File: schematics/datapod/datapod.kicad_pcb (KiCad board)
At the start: 2 copper layers, 152.7 x 152.7 mm, 56 parts, among them J1 Conn_01x02, J2 Conn_02x03_Odd_Even, J3 Conn_01x02, J4 DB9_Female, J5 DB9_Male_MountingHoles, J6 Micro_SD_Card, J7 Conn_02x02_Odd_Even, J8 Conn_01x02_Female, K1 DS2E-SL2-DC5V, K2 DS2E-SL2-DC5V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

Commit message: made 1st pcb
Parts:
- moved J3 106.8 mm to (123.2, 149.9), turned to 203 degrees
- moved D3 105.4 mm to (114.3, 25.4), turned to 0 degrees
- moved J7 102.8 mm to (48.3, 141.0), turned to 45 degrees
- moved C1 97.3 mm to (144.6, 119.3), turned to 315 degrees
- moved J8 92.8 mm to (48.3, 59.7), turned to 236 degrees
- moved D1 92.3 mm to (85.6, 149.9), turned to 180 degrees
- moved Q4 90.7 mm to (158.8, 135.9)
- moved D4 87.8 mm to (110.5, 52.6), turned to 270 degrees
- moved D5 87.2 mm to (72.1, 75.3)
- moved C17 85.0 mm to (82.4, 62.1), turned to 90 degrees
- moved C14 84.9 mm to (73.2, 78.9)
- moved Q2 84.0 mm to (120.7, 61.0)
- moved RN1 82.9 mm to (158.8, 124.5), turned to 180 degrees
- moved C7 81.9 mm to (167.6, 122.9), turned to 90 degrees
- moved Q3 80.4 mm to (151.1, 108.0), turned to 180 degrees
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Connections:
- RN1 pad 10: VcR1 -> Net-(RN1-Pad10)
- RN3 pad 10: Net-(RN3-Pad10) -> VcR1
- RN3 pad 11: Net-(RN3-Pad11) -> GND
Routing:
- net VCC: track 0.00 -> 122.9 mm, vias 0 -> 3
- net GND: track 0.00 -> 99.7 mm
- net Net-(C12-Pad2): track 0.00 -> 49.5 mm
- net RELAY2_OFF: track 0.00 -> 43.4 mm, vias 0 -> 2
- net +5V: track 0.00 -> 40.9 mm, vias 0 -> 4
- net +3V3: track 0.00 -> 40.5 mm, vias 0 -> 1
- net RELAY2_ON: track 0.00 -> 25.3 mm, vias 0 -> 1
- net MICRO_SD_MOSI: track 0.00 -> 24.1 mm
- net Net-(J4-Pad2): track 0.00 -> 17.9 mm
- net Net-(J4-Pad3): track 0.00 -> 17.3 mm
- net Net-(C2-Pad1): track 0.00 -> 16.9 mm
- net MCU-SDA: track 0.00 -> 16.6 mm
- net MICRO_SD_MISO: track 0.00 -> 15.9 mm
- net Net-(C10-Pad2): track 0.00 -> 15.4 mm
- net MICRO_SD_SCK: track 0.00 -> 15.3 mm
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- added copper zone on F.Cu, net +3V3
- added copper zone on F.Cu, net +5V
- added copper zone on F.Cu, net Net-(C14-Pad2)
- added copper zone on F.Cu, net Net-(C9-Pad2)

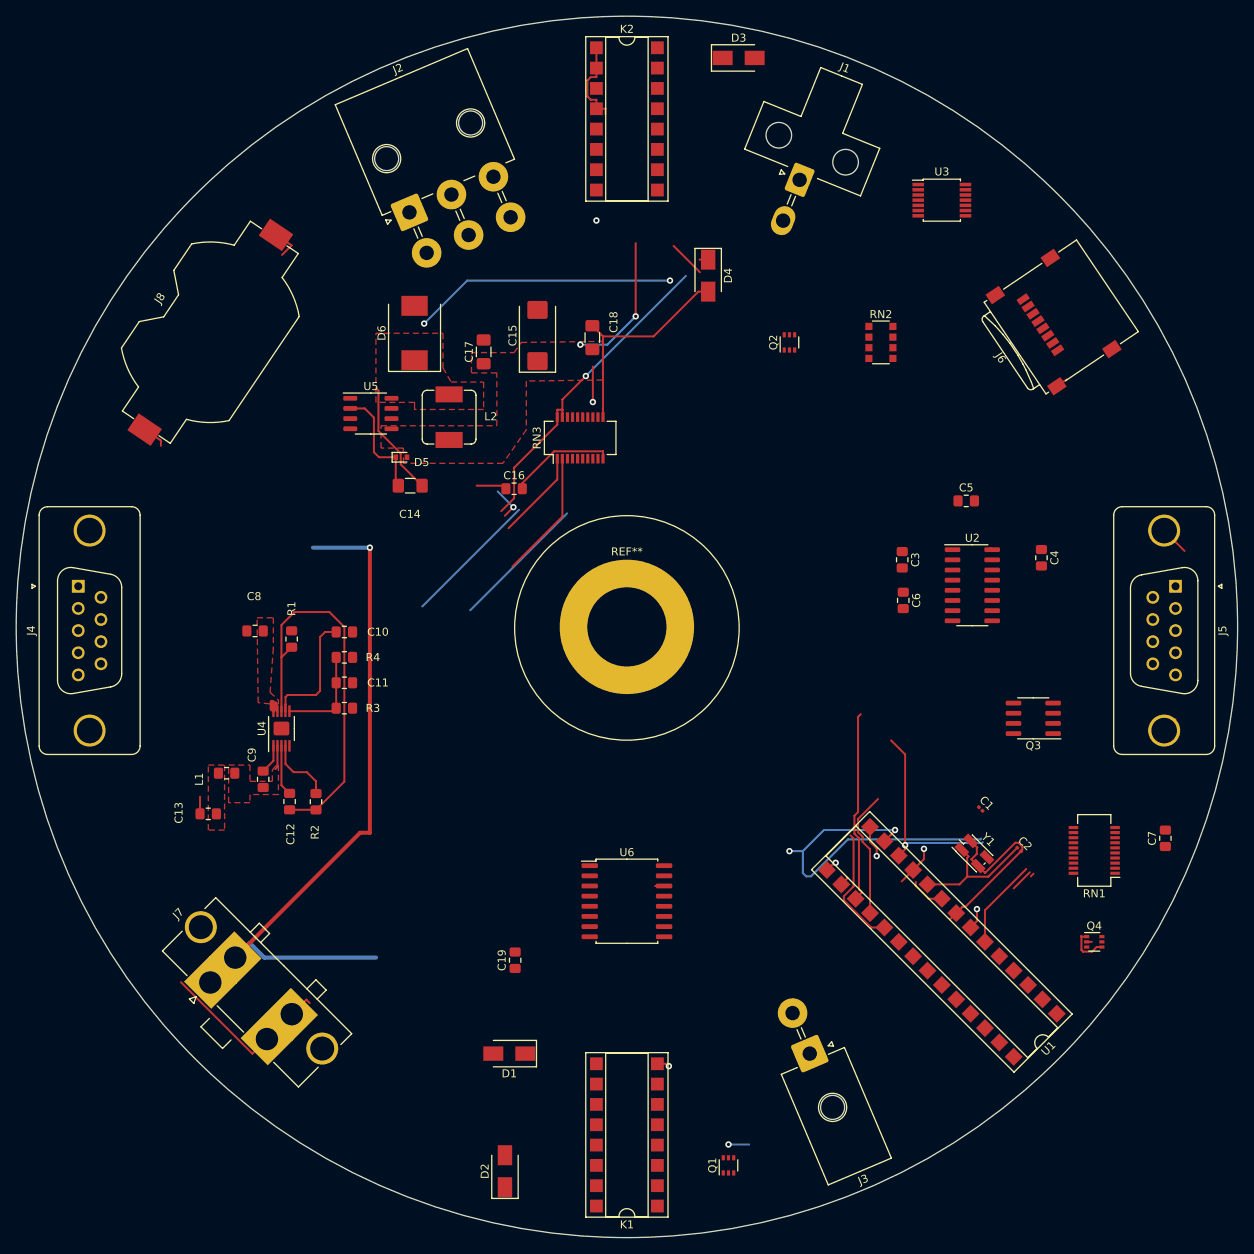
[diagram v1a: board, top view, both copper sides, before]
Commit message: finished routing now removing warnings
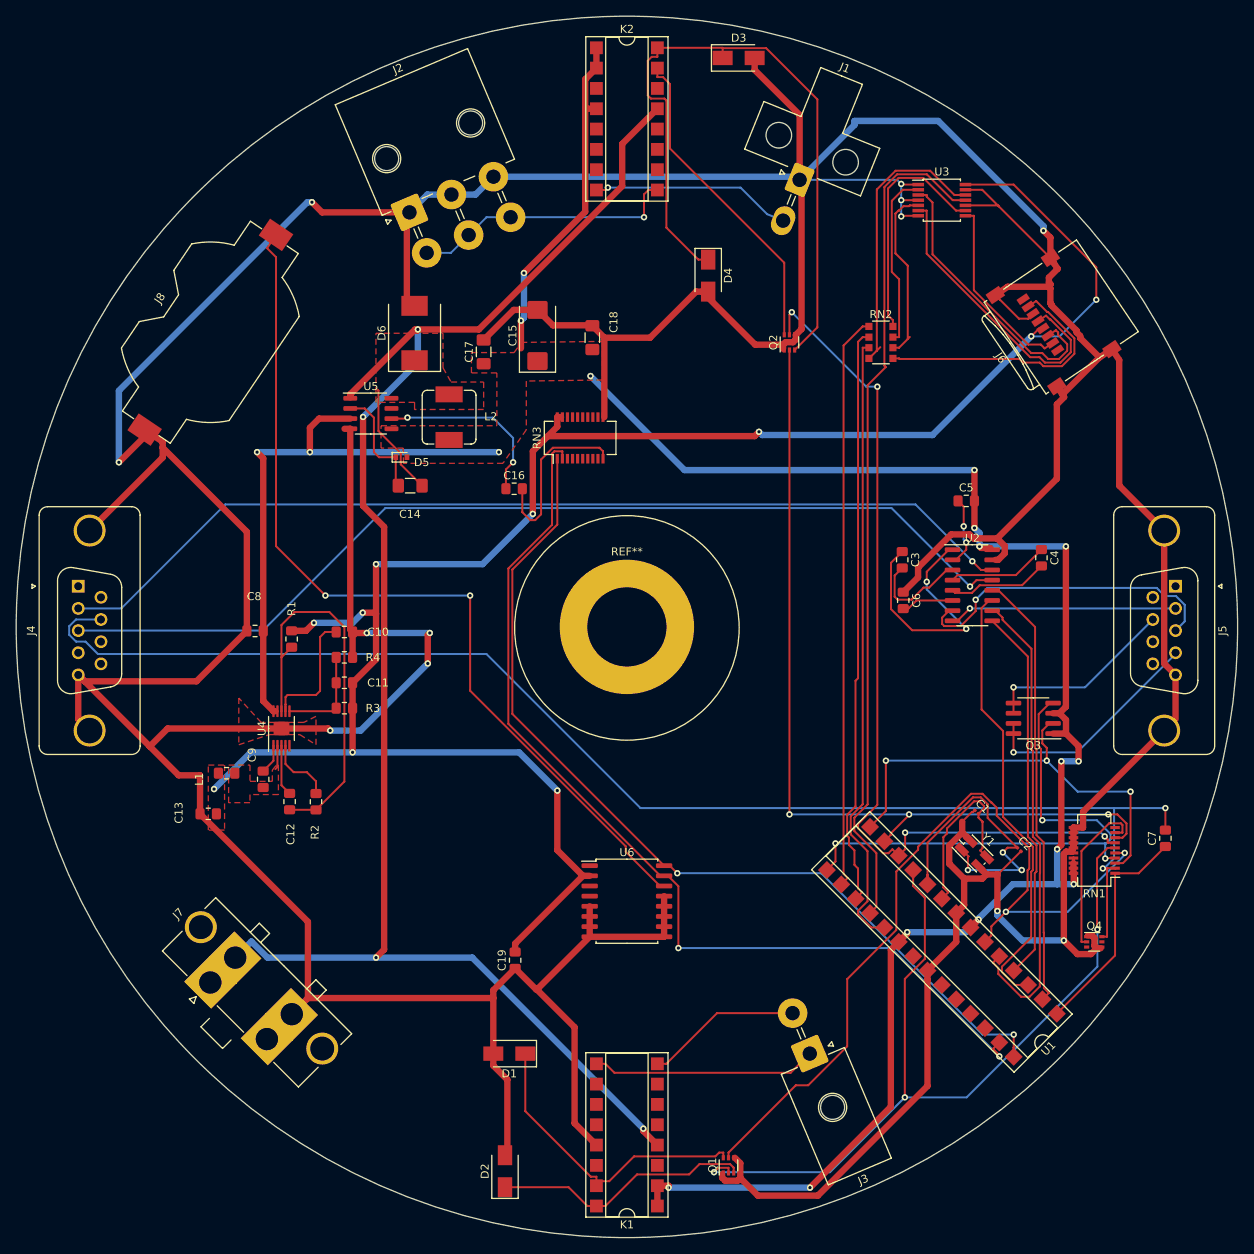
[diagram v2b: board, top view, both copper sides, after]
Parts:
- moved C1 0.64 mm to (144.0, 119.7)
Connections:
- J4 pad 0: (no net) -> GND
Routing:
- net GND: track 99.7 -> 909.6 mm, vias 0 -> 12
- net +5V: track 40.9 -> 326.1 mm, vias 4 -> 18
- net +3V3: track 40.5 -> 247.6 mm, vias 1 -> 10
- net DRAIN_PROG: track 0.61 -> 173.3 mm, vias 0 -> 2
- net MCU-SDA: track 16.6 -> 124.5 mm, vias 0 -> 2
- net Net-(J4-Pad3): track 17.3 -> 125.0 mm, vias 0 -> 1
- net MCU-SCL: track 11.7 -> 117.4 mm, vias 0 -> 2
- net Net-(J4-Pad2): track 17.9 -> 123.4 mm, vias 0 -> 1
- net Net-(J8-Pad1): track 9.51 -> 113.2 mm, vias 1 -> 2
- net RELAY1_OFF: track 5.35 -> 108.7 mm, vias 1 -> 3
- net MICRO_SD_MISO: track 15.9 -> 106.6 mm
- net RELAY1_ON: track 13.8 -> 102.9 mm, vias 1 -> 2
- net Net-(D3-Pad1): track 1.08 -> 88.6 mm
- net RELAY2_ON: track 25.3 -> 111.4 mm, vias 1 -> 4
- net VCC: track 122.9 -> 208.7 mm, vias 3 -> 4
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- added copper zone on F.Cu, net GND

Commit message: added final routed PCB, gerbers and BOM
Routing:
- net MICRO_SD_SCK: track 77.6 -> 109.4 mm, vias 0 -> 4
- net Net-(J6-Pad7): track 34.2 -> 23.5 mm, vias 0 -> 2
- net RELAY1_ON: track 102.9 -> 95.8 mm, vias 2 -> 5
- net MICRO_SD_MOSI: track 73.4 -> 74.5 mm
- net GND: vias 12 -> 34
- added copper zone on B.Cu, net GND
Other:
- board text added: "AOML ABIISS Datapod module Rev. 1"
